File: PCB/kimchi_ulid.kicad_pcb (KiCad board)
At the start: 4 copper layers, 65 x 45.4 mm, 49 parts, among them J1 RCJ-2123, J2 DF40HC(3.5)-60DS, J3 DF40HC(3.5)-60DS, J4 RCJ-2123, J5 54-00176, J6 Conn_01x03_Male, U1 24C32, U2 WM8750CJLGEFL, U3 SN74LV1T34DBVRG4, X1 ASFL1-12.288MHZ-EC-T

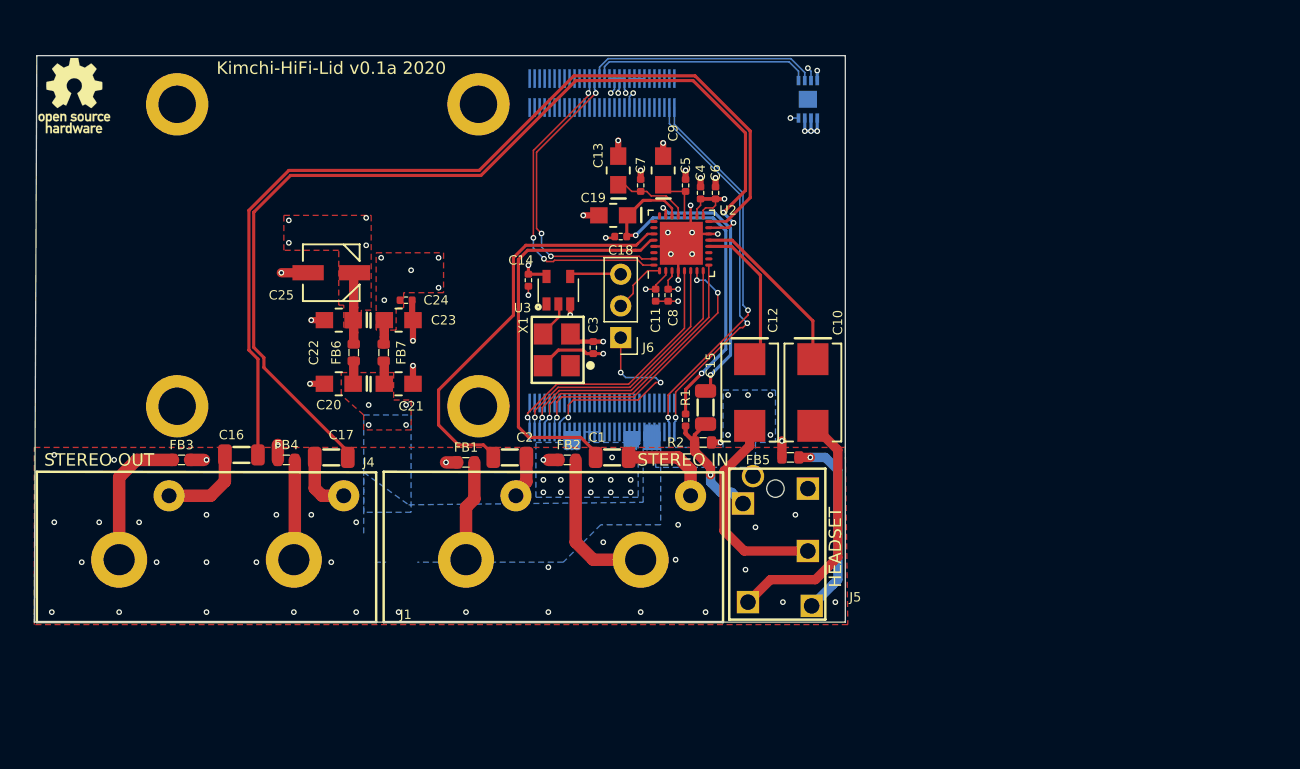
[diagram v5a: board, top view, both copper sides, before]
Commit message: PCB tweaks
fixed crooked board edge. Corrected board dimension labels. Moved board inside project so that bottom left corner is the origin.
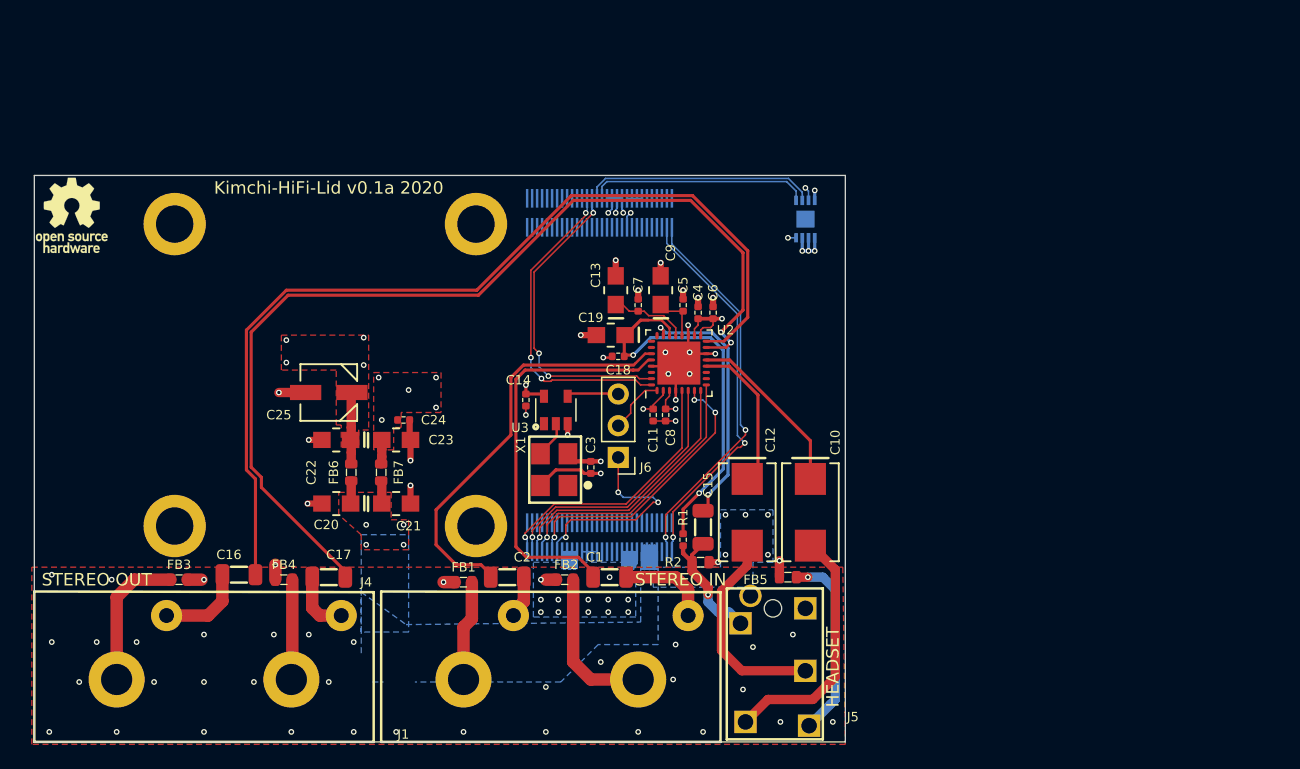
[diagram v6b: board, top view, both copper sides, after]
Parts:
- moved C19 9.60 mm to (153.2, 93.4)
- moved C20 9.60 mm to (131.2, 106.9)
- moved C21 9.60 mm to (136.0, 106.9)
- moved C24 9.60 mm to (136.6, 100.2)
- moved FB1 9.60 mm to (141.4, 113.2)
- moved FB6 9.60 mm to (132.4, 104.4)
- moved FB7 9.60 mm to (134.8, 104.4)
- moved H3 9.60 mm to (118.2, 108.7)
- moved H4 9.60 mm to (142.4, 108.7)
- moved J6 9.60 mm to (153.8, 103.2)
- moved U3 9.60 mm to (148.8, 99.4)
- moved X1 9.60 mm to (148.7, 104.2)
- moved C1 9.60 mm to (153.1, 112.8)
- moved C10 9.60 mm to (169.2, 107.6)
- moved C11 9.60 mm to (156.6, 99.8)
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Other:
- outline, holes or cut-outs redrawn

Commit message: Fab FIles
Fab files generated
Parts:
- added L1: GG_LOGO, kimchi_ulid:groupgets_logo, F.Cu at (111.4, 93.2)
- added L2: OSHPARK_LOGO, kimchi_ulid:oshpark_logo, F.Cu at (111.4, 101.6)
- moved LOGO1 1.41 mm to (111.4, 84.0)
